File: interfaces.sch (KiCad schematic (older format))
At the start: 101 parts, among them J6 0878311420, J7 61300611121, U1 MTFC16GAPALNA-AIT, U14 XC7A100T-FGG484, U17 USB3300-EZK-TR, U18 USB3300-EZK-TR, U6 NVT2008DQ,115, Y1 TSX-3225, Y3 TSX-3225

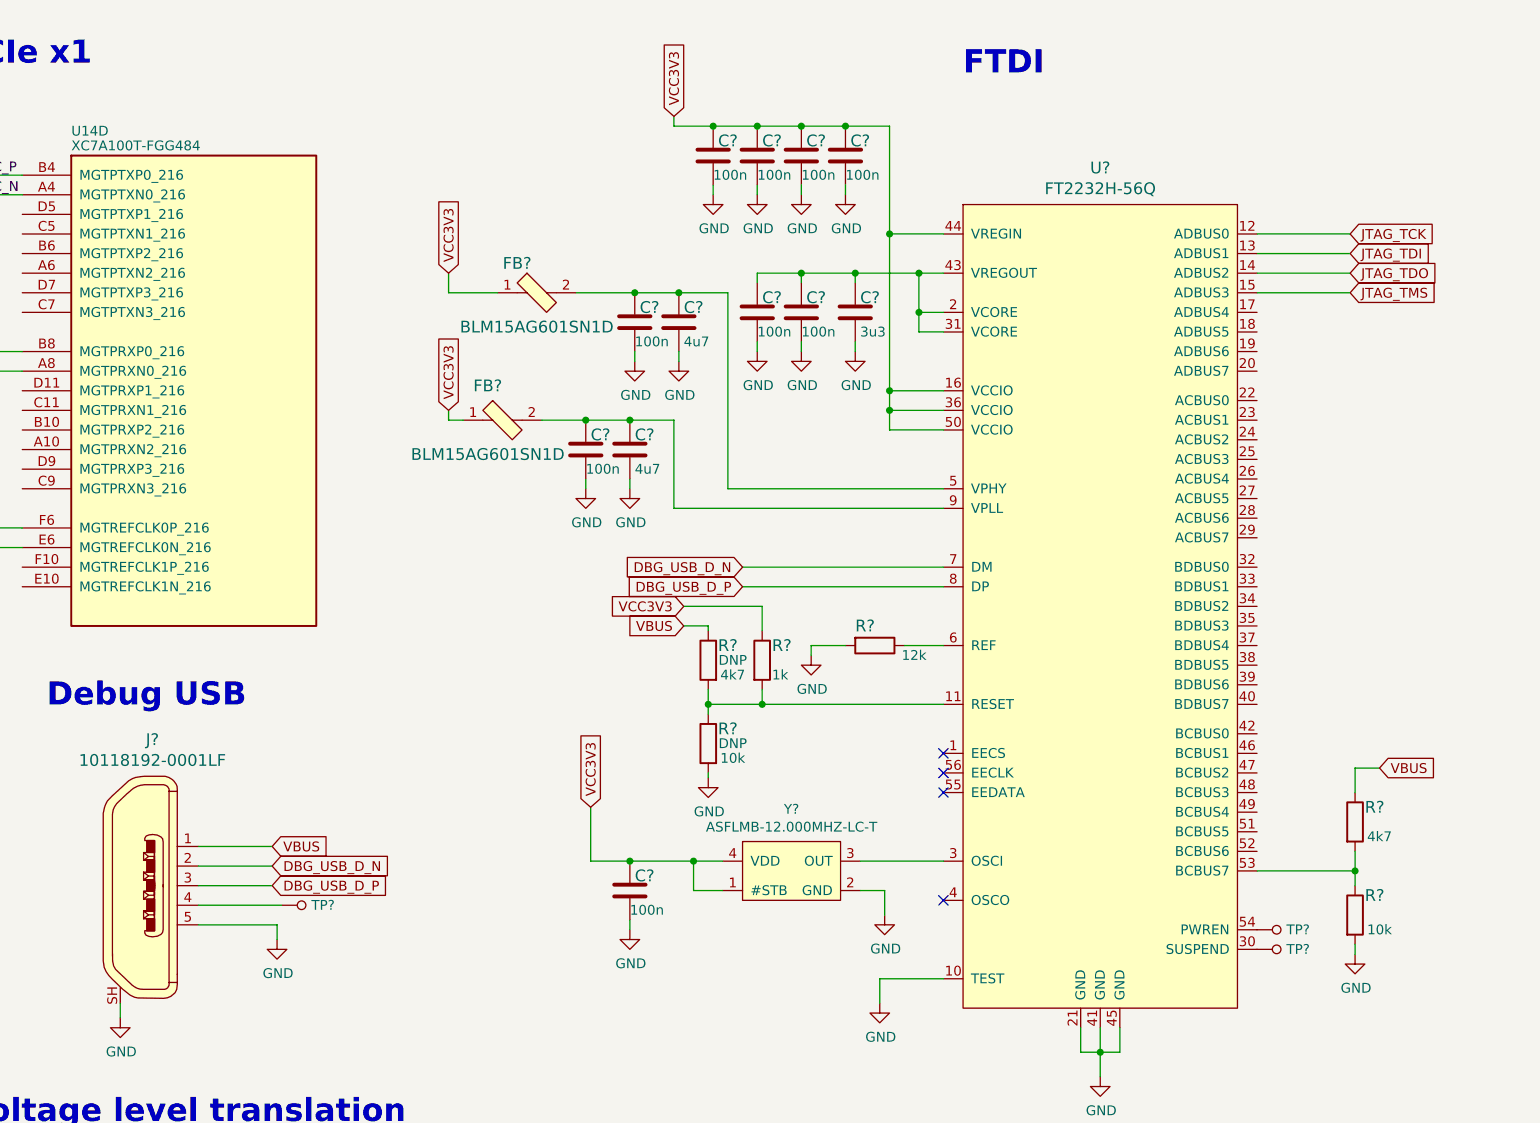
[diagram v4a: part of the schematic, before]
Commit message: Routed FTDI/JTAG
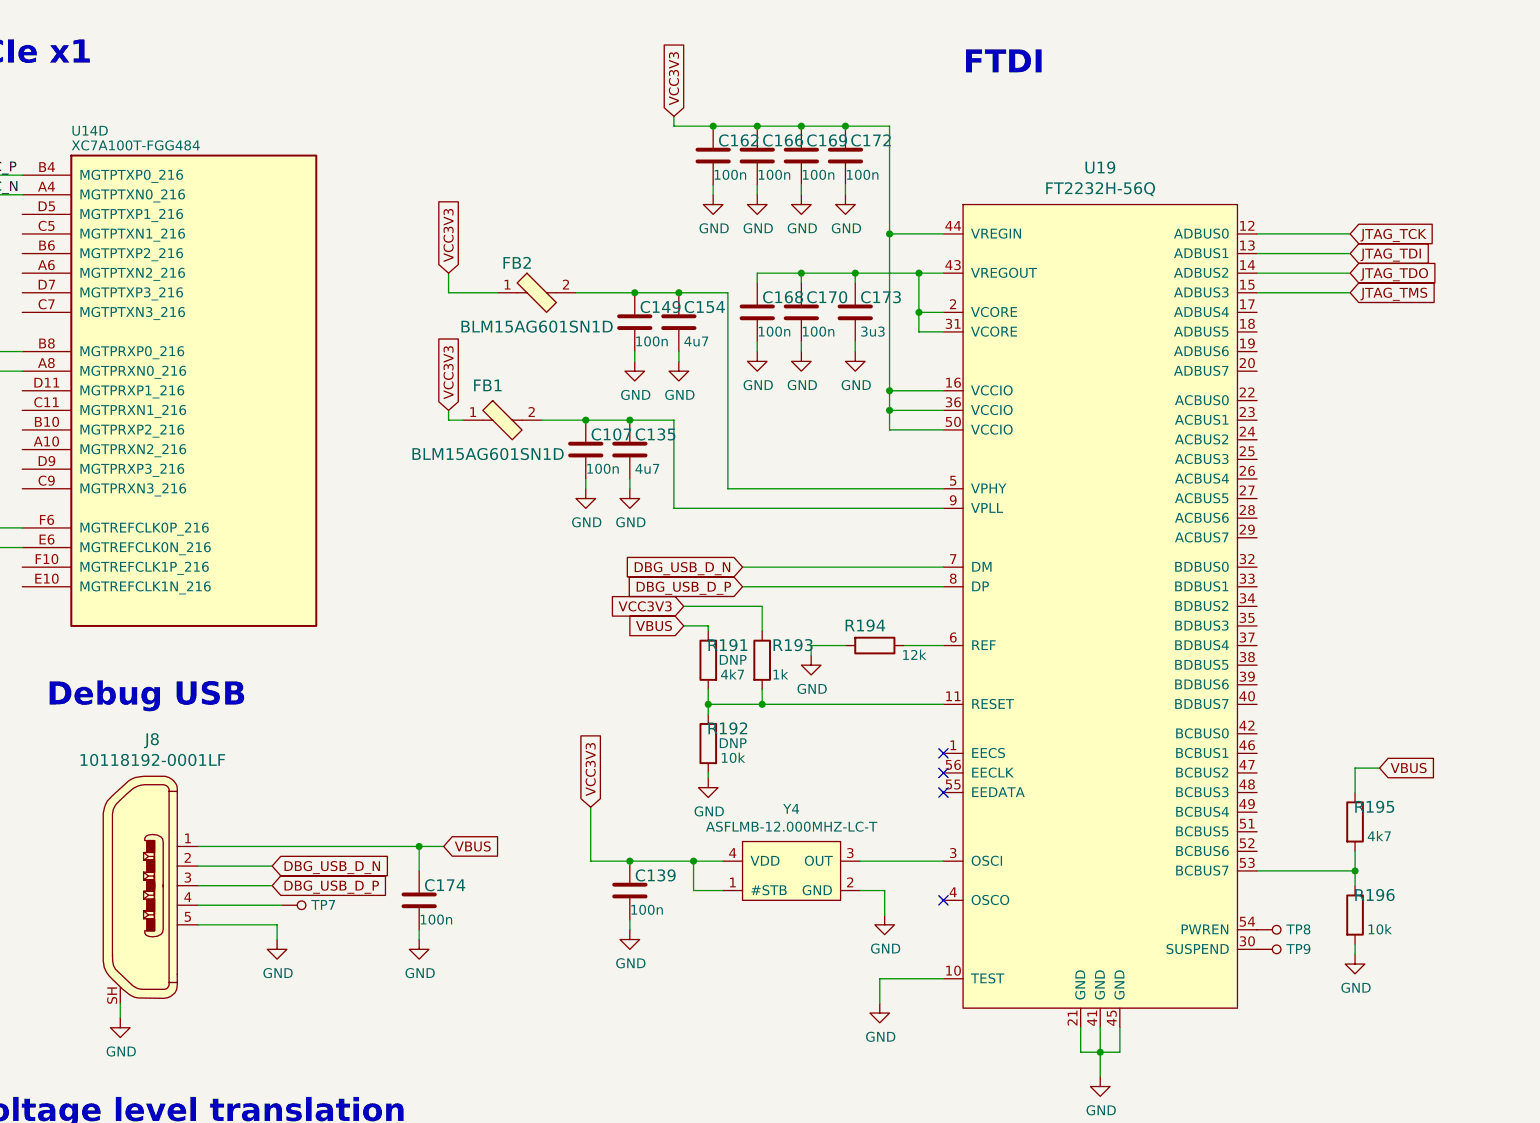
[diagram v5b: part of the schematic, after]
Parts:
- added C174: C_100n_0402, artix-dc-scm-footprints:0402-cap, symbol artix-dc-scm:C_100n_0402
- gave numbers to parts that had none: 26
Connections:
- net GND: now also C174.2
- net VBUS: now also C174.1

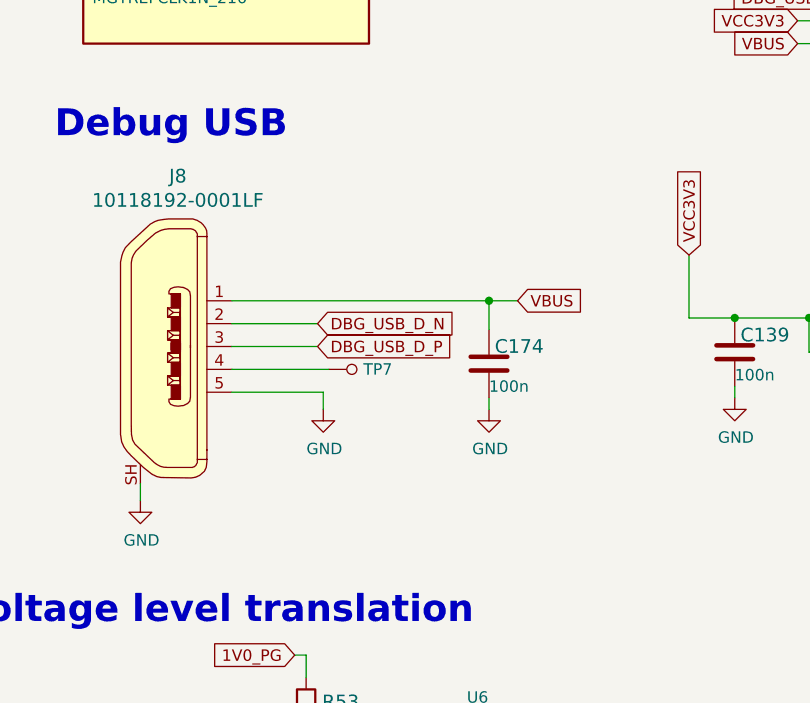
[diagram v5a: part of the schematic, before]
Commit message: Update USB 3d model and add VBUS decoupling
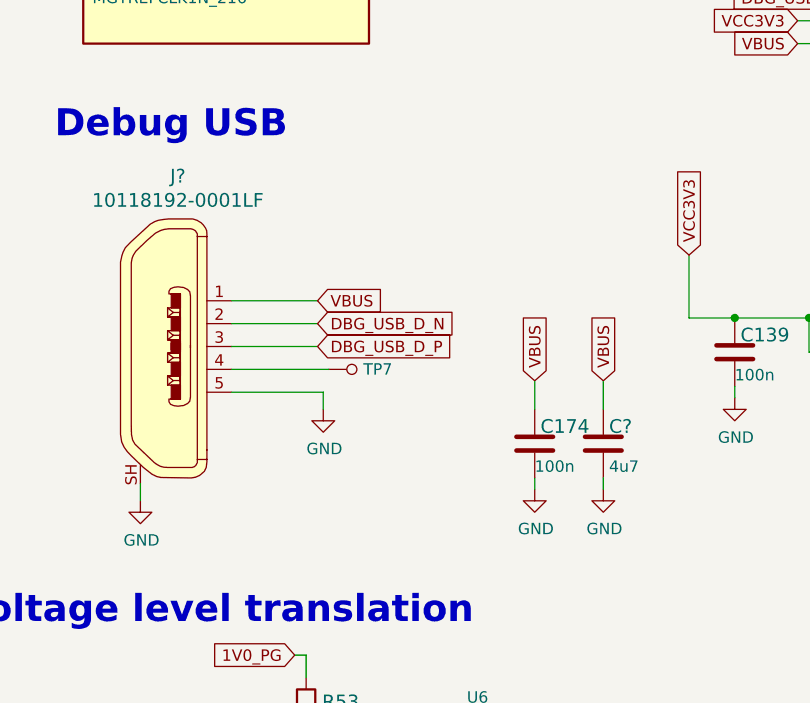
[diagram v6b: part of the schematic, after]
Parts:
- removed J8: 10118192-0001LF, artix-dc-scm-footprints:USB_Micro_B_Female_10118192, symbol artix-dc-scm:10118192-0001LF
- added C?: C_4u7_0402, artix-dc-scm-footprints:0402-cap, symbol artix-dc-scm:C_4u7_0402
- added J?: 10118192-0001LF, antmicro-footprints:USB_Micro_B_Female_10118192, symbol antmicroUSBDVIHDMIConnectors:10118192-0001LF
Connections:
- net DBG_USB_D_N: now also J?.2
- net DBG_USB_D_P: now also J?.3
- net GND: now also C?.2, J?.5, J?.SH
- net VBUS: now also C?.1, J?.1
- net at TP7.1: now also J?.4
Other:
- moved on the sheet: C174
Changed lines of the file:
@@
 Wire Wire Line
 	5525 4875 5325 4875
-$Comp
-L artix-dc-scm:10118192-0001LF J?
-U 1 1 606A4BD2
-P 3025 5000
-AR Path="/614223A1/60643A57/606A4BD2" Ref="J?"  Part="1"
-AR Path="/614223A1/606A4BD2" Ref="J8"  Part="1"
-F 0 "J8" H 3089 5745 60  0000 C CNN
-F 1 "10118192-0001LF" H 3089 5639 60  0000 C CNN
-F 2 "artix-dc-scm-footprints:USB_Micro_B_Female_10118192" H 3225 5200 60  0001 L CNN
-F 3 "http://www.amphenol-icc.com/media/wysiwyg/files/drawing/10118192.pdf" H 3225 5300 60  0001 L CNN
-F 4 "10118192-0001LF" H 3225 5500 60  0001 L CNN "MPN"
-F 5 "Amphenol ICC (FCI)" H 3225 6100 60  0001 L CNN "Manufacturer"
-	1    3025 5000
-	1    0    0    -1
-$EndComp
 Wire Wire Line
 	3325 5200 3725 5200
@@
 L artix-dc-scm:C_100n_0402 C?
 U 1 1 6022FF73
-P 4450 5075
+P 4650 5425
 AR Path="/614223A1/60643A57/6022FF73" Ref="C?"  Part="1"
 AR Path="/614223A1/6022FF73" Ref="C174"  Part="1"
-F 0 "C174" H 4475 5150 60  0000 L CNN
-F 1 "C_100n_0402" H 4450 4925 60  0001 C CNN
-F 2 "artix-dc-scm-footprints:0402-cap" H 4650 5275 60  0001 L CNN
-F 3 "" H 4450 5075 50  0001 C CNN
-F 4 "Walsin" H 4650 5475 60  0001 L CNN "Manufacturer"
-F 5 "0402X104K6R3CT" H 4650 5375 60  0001 L CNN "MPN"
-F 6 "100n" H 4450 4975 50  0000 L CNN "Val"
-	1    4450 5075
-	1    0    0    -1
-$EndComp
-Wire Wire Line
-	4450 5225 4450 5275
+F 0 "C174" H 4675 5500 60  0000 L CNN
+F 1 "C_100n_0402" H 4650 5275 60  0001 C CNN
+F 2 "artix-dc-scm-footprints:0402-cap" H 4850 5625 60  0001 L CNN
+F 3 "" H 4650 5425 50  0001 C CNN
+F 4 "Walsin" H 4850 5825 60  0001 L CNN "Manufacturer"
+F 5 "0402X104K6R3CT" H 4850 5725 60  0001 L CNN "MPN"
+F 6 "100n" H 4650 5325 50  0000 L CNN "Val"
+	1    4650 5425
+	1    0    0    -1
+$EndComp
+Wire Wire Line
+	4650 5575 4650 5625
 $Comp
 L artix-dc-scm:GND-artix-dc-scm #PWR0149
 U 1 1 6022FF7A
-P 4450 5275
-F 0 "#PWR0149" H 4450 5025 50  0001 C CNN
-F 1 "GND" H 4455 5102 50  0000 C CNN
-F 2 "" H 4450 5275 50  0001 C CNN
-F 3 "" H 4450 5275 50  0001 C CNN
-	1    4450 5275
-	1    0    0    -1
-$EndComp
-Text GLabel 4575 4800 2    50   Input ~ 0
+P 4650 5625
+F 0 "#PWR0149" H 4650 5375 50  0001 C CNN
+F 1 "GND" H 4655 5452 50  0000 C CNN
+F 2 "" H 4650 5625 50  0001 C CNN
+F 3 "" H 4650 5625 50  0001 C CNN
+	1    4650 5625
+	1    0    0    -1
+$EndComp
+Text GLabel 3700 4800 2    50   Input ~ 0
 VBUS
 Wire Wire Line
-	3325 4800 4450 4800
-Wire Wire Line
-	4450 4925 4450 4800
-Connection ~ 4450 4800
-Wire Wire Line
-	4450 4800 4575 4800
+	4650 5275 4650 5150
+$Comp
+L antmicroUSBDVIHDMIConnectors:10118192-0001LF J?
+U 1 1 60109106
+P 3025 5000
+F 0 "J?" H 3089 5745 60  0000 C CNN
+F 1 "10118192-0001LF" H 3089 5639 60  0000 C CNN
+F 2 "antmicro-footprints:USB_Micro_B_Female_10118192" H 3225 5200 60  0001 L CNN
+F 3 "http://www.amphenol-icc.com/media/wysiwyg/files/drawing/10118192.pdf" H 3225 5300 60  0001 L CNN
+F 4 "10118192-0001LF" H 3225 5500 60  0001 L CNN "MPN"
+F 5 "Amphenol ICC (FCI)" H 3225 6100 60  0001 L CNN "Manufacturer"
+	1    3025 5000
+	1    0    0    -1
+$EndComp
+Wire Wire Line
+	3325 4800 3700 4800
+Text GLabel 4650 5150 1    50   Input ~ 0
+VBUS
+$Comp
+L artix-dc-scm:C_4u7_0402 C?
+U 1 1 601C3138
+P 4950 5425
+AR Path="/614223A1/60643A57/601C3138" Ref="C?"  Part="1"
+AR Path="/614223A1/601C3138" Ref="C?"  Part="1"
+F 0 "C?" H 4975 5500 60  0000 L CNN
+F 1 "C_4u7_0402" H 4950 5275 60  0001 C CNN
+F 2 "artix-dc-scm-footprints:0402-cap" H 5150 5625 60  0001 L CNN
+F 3 "" H 4950 5425 50  0001 C CNN
+F 4 "MURATA" H 5150 5825 60  0001 L CNN "Manufacturer"
+F 5 "GRM155R61A475MEAAD" H 5150 5725 60  0001 L CNN "MPN"
+F 6 "4u7" H 4975 5325 50  0000 L CNN "Val"
+	1    4950 5425
+	1    0    0    -1
+$EndComp
+Wire Wire Line
+	4950 5575 4950 5625
+$Comp
+L artix-dc-scm:GND-artix-dc-scm #PWR?
+U 1 1 601C313F
+P 4950 5625
+F 0 "#PWR?" H 4950 5375 50  0001 C CNN
+F 1 "GND" H 4955 5452 50  0000 C CNN
+F 2 "" H 4950 5625 50  0001 C CNN
+F 3 "" H 4950 5625 50  0001 C CNN
+	1    4950 5625
+	1    0    0    -1
+$EndComp
+Wire Wire Line
+	4950 5275 4950 5150
+Text GLabel 4950 5150 1    50   Input ~ 0
+VBUS
 $EndSCHEMATC

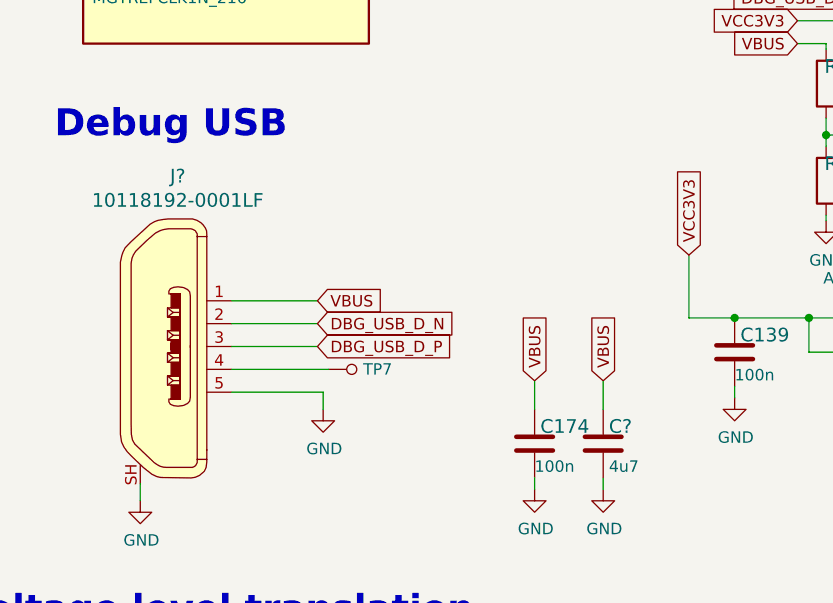
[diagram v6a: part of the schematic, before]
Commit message: Bumped revision to 1.0.1 - replaced ROT connector, added ROT signals and connected to FPGA
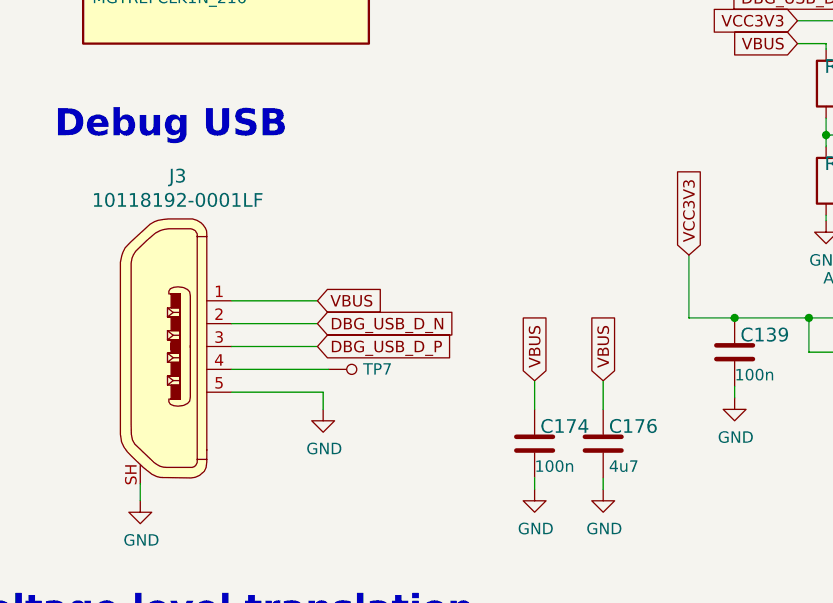
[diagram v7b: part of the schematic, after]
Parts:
- gave numbers to parts that had none: 2
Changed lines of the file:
@@
 Title "Artix - Datacenter Secure Control Module (DC-SCM)"
 Date ""
-Rev "1.0.0"
+Rev "1.0.1"
 Comp ""
 Comment1 ""
@@
 	4650 5275 4650 5150
 $Comp
-L antmicroUSBDVIHDMIConnectors:10118192-0001LF J?
+L antmicroUSBDVIHDMIConnectors:10118192-0001LF J3
 U 1 1 60109106
 P 3025 5000
-F 0 "J?" H 3089 5745 60  0000 C CNN
+F 0 "J3" H 3089 5745 60  0000 C CNN
 F 1 "10118192-0001LF" H 3089 5639 60  0000 C CNN
 F 2 "antmicro-footprints:USB_Micro_B_Female_10118192" H 3225 5200 60  0001 L CNN
@@
 P 4950 5425
 AR Path="/614223A1/60643A57/601C3138" Ref="C?"  Part="1"
-AR Path="/614223A1/601C3138" Ref="C?"  Part="1"
-F 0 "C?" H 4975 5500 60  0000 L CNN
+AR Path="/614223A1/601C3138" Ref="C176"  Part="1"
+F 0 "C176" H 4975 5500 60  0000 L CNN
 F 1 "C_4u7_0402" H 4950 5275 60  0001 C CNN
 F 2 "artix-dc-scm-footprints:0402-cap" H 5150 5625 60  0001 L CNN
@@
 	4950 5575 4950 5625
 $Comp
-L artix-dc-scm:GND-artix-dc-scm #PWR?
+L artix-dc-scm:GND-artix-dc-scm #PWR0150
 U 1 1 601C313F
 P 4950 5625
-F 0 "#PWR?" H 4950 5375 50  0001 C CNN
+F 0 "#PWR0150" H 4950 5375 50  0001 C CNN
 F 1 "GND" H 4955 5452 50  0000 C CNN
 F 2 "" H 4950 5625 50  0001 C CNN

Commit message: Update edge connector
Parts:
- J3: footprint antmicro-footprints:USB_Micro_B_Female_10118192 -> artix-dc-scm-footprints:USB_Micro_B_Female_10118192; symbol antmicroUSBDVIHDMIConnectors:10118192-0001LF -> artix-dc-scm:10118192-0001LF
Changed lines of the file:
@@
 	4650 5275 4650 5150
 $Comp
-L antmicroUSBDVIHDMIConnectors:10118192-0001LF J3
+L artix-dc-scm:10118192-0001LF J3
 U 1 1 60109106
 P 3025 5000
 F 0 "J3" H 3089 5745 60  0000 C CNN
 F 1 "10118192-0001LF" H 3089 5639 60  0000 C CNN
-F 2 "antmicro-footprints:USB_Micro_B_Female_10118192" H 3225 5200 60  0001 L CNN
+F 2 "artix-dc-scm-footprints:USB_Micro_B_Female_10118192" H 3225 5200 60  0001 L CNN
 F 3 "http://www.amphenol-icc.com/media/wysiwyg/files/drawing/10118192.pdf" H 3225 5300 60  0001 L CNN
 F 4 "10118192-0001LF" H 3225 5500 60  0001 L CNN "MPN"
